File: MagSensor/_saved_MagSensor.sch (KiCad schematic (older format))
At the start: 0 parts

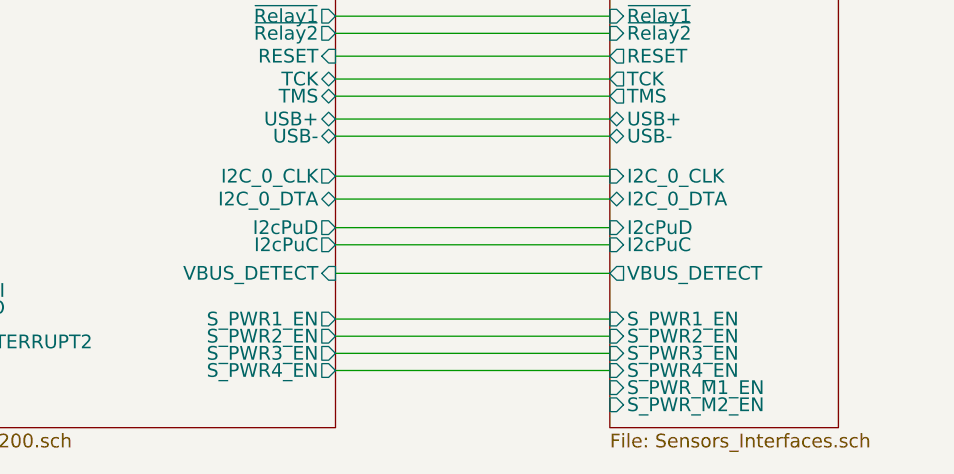
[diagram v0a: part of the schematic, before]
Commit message: Six sensor system DRC and ERC completed
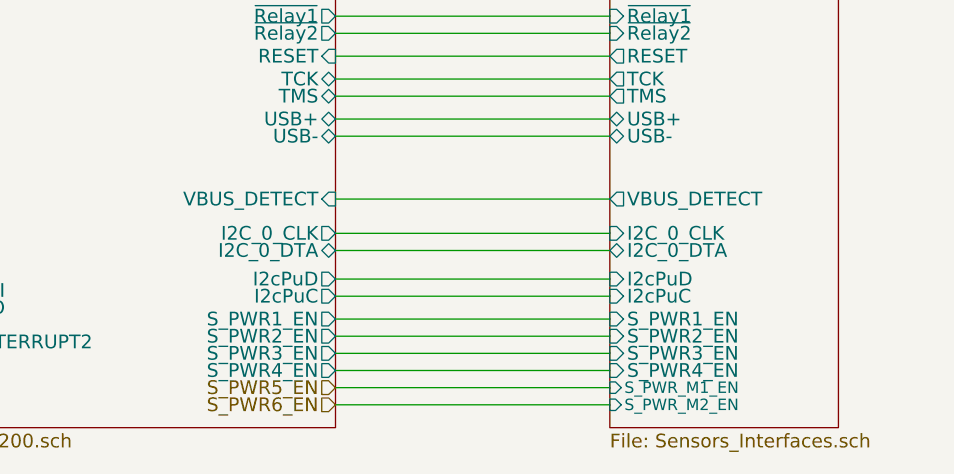
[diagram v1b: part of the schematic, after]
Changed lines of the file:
@@
 EESchema Schematic File Version 4
-LIBS:MagSensor-cache
-EELAYER 29 0
+EELAYER 26 0
 EELAYER END
 $Descr A4 11693 8268
@@
 F20 "~Relay2" O R 6975 4025 60
 F21 "~LCD_BACKLIGHT_PWM" O L 5075 3400 60
-F22 "I2C_0_CLK" O R 6975 4650 60
-F23 "I2C_0_DTA" B R 6975 4750 60
-F24 "VBUS_DETECT" I R 6975 5075 60
-F25 "I2cPuD" O R 6975 4875 60
-F26 "I2cPuC" O R 6975 4950 60
+F22 "I2C_0_CLK" O R 6975 4900 60
+F23 "I2C_0_DTA" B R 6975 4975 60
+F24 "VBUS_DETECT" I R 6975 4750 60
+F25 "I2cPuD" O R 6975 5100 60
+F26 "I2cPuC" O R 6975 5175 60
 F27 "LCD_EN" O L 5075 3200 60
 F28 "~LCD_RESET" O L 5075 3500 60
@@
 F7 "~Relay1" I L 8175 3950 60
 F8 "~Relay2" I L 8175 4025 60
-F9 "VBUS_DETECT" O L 8175 5075 60
-F10 "I2C_0_DTA" B L 8175 4750 60
-F11 "I2C_0_CLK" I L 8175 4650 60
-F12 "I2cPuC" I L 8175 4950 60
-F13 "I2cPuD" I L 8175 4875 60
+F9 "VBUS_DETECT" O L 8175 4750 60
+F10 "I2C_0_DTA" B L 8175 4975 60
+F11 "I2C_0_CLK" I L 8175 4900 60
+F12 "I2cPuC" I L 8175 5175 60
+F13 "I2cPuD" I L 8175 5100 60
 F14 "S_PWR1_EN" I L 8175 5275 60
 F15 "S_PWR2_EN" I L 8175 5350 60
 F16 "S_PWR3_EN" I L 8175 5425 60
 F17 "S_PWR4_EN" I L 8175 5500 60
-F18 "S_PWR_M1_EN" I L 8175 5575 60
-F19 "S_PWR_M2_EN" I L 8175 5650 60
+F18 "S_PWR_M1_EN" I L 8175 5575 50
+F19 "S_PWR_M2_EN" I L 8175 5650 50
 $EndSheet
 Wire Wire Line
@@
 	6975 4475 8175 4475
 Wire Wire Line
-	6975 4650 8175 4650
-Wire Wire Line
-	6975 4750 8175 4750
-Wire Wire Line
-	6975 5075 8175 5075
-Wire Wire Line
-	6975 4875 8175 4875
-Wire Wire Line
-	6975 4950 8175 4950
+	6975 4900 8175 4900
+Wire Wire Line
+	6975 4975 8175 4975
+Wire Wire Line
+	6975 5100 8175 5100
+Wire Wire Line
+	6975 5175 8175 5175
 Wire Wire Line
 	6975 5275 8175 5275
@@
 Wire Wire Line
 	6975 2575 7600 2575
+Wire Wire Line
+	8175 4750 6975 4750
+Text HLabel 6975 5575 0    60   Input ~ 0
+S_PWR5_EN
+Text HLabel 6975 5650 0    60   Input ~ 0
+S_PWR6_EN
+Wire Wire Line
+	6975 5575 8175 5575
+Wire Wire Line
+	6975 5650 8175 5650
 $EndSCHEMATC
